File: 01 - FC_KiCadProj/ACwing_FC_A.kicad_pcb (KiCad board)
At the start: 4 copper layers, 40.8 x 40.8 mm, 111 parts, among them J1 USB-C (HRO TYPE-C-31-M-12), J2 ESC link, J3 Qwiic, J4 Qwiic, J5 ELRS, J6 ESC link B, J7 VBAT+, J8 GND, Q5 AO3401A, U1 LSM6DSV16X, U10 W25Q128JV, U11 LDK130PU-R, U12 LM5166DRCT, U13 SN74LV1T34DCKR, U2 STM32WB55CGU6, U3 IIS2MDC, U4 LPS22HH, U5 LD39130SPUR, U7 USBLC6-2SC6, U8 MLPF-WB55-01E3, Y1 32MHz

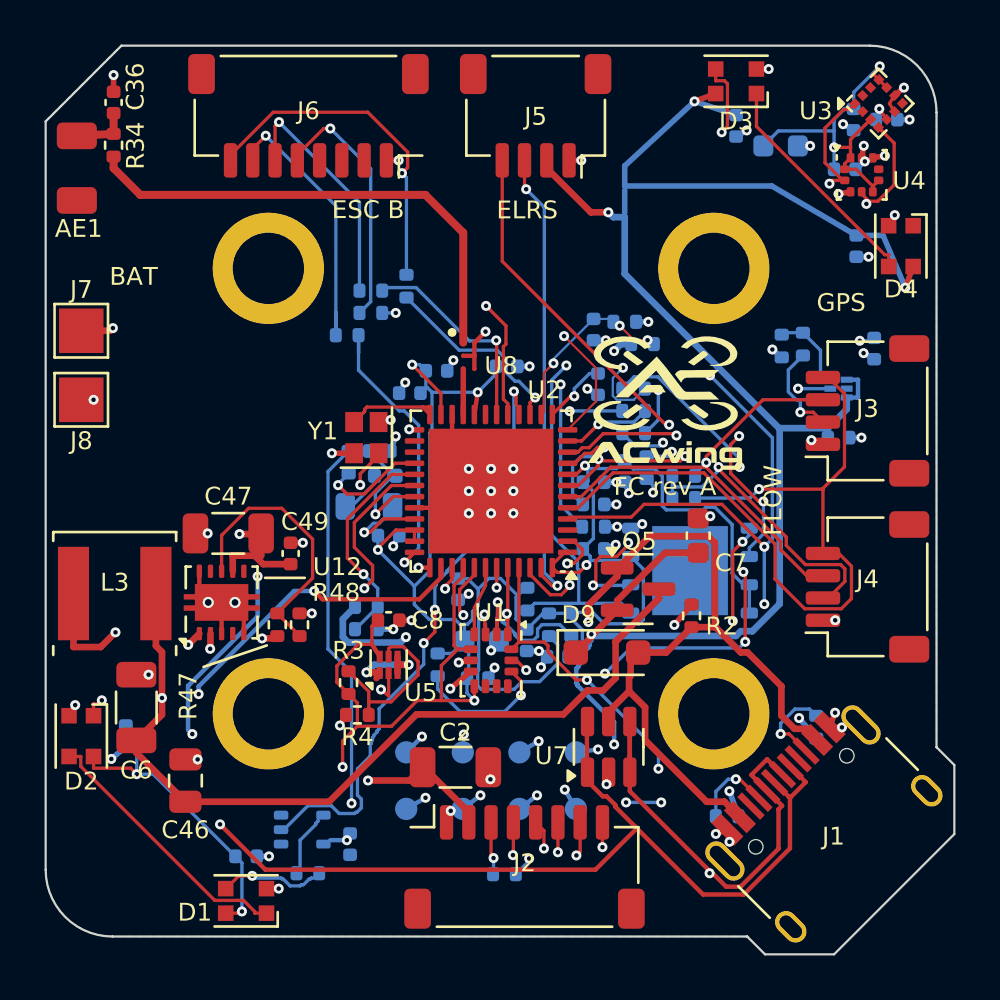
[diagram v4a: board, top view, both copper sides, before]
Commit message: Silkscreen review: board names, connector labels on the right side
- Board name + revision only, same on every board and layer: "FC rev A",
  "ESC 1S rev A", "GPS rev A", "Flow rev A" (was "ACwing ... rev A" on some).
- FC: USB and ESC A labels moved to the top (with J1 / J2); GPS and FLOW
  centred on J3 / J4; ESC B and ELRS on one line; BAT beside J7 / J8.
- Same fix on ESC 1S (CHARGE to the top, TO FC centred on J1) and GPS
  (QWIIC IN / OUT to the top, outside the SAM-M10Q outline).
- silk_brand.py: labels stay on the connector's side and never under a part;
  brand README rules updated. Gerbers, DRC (0 / 0 on all boards), views.

Co-Authored-By: Claude Opus 5.5 <noreply@anthropic.com>
Claude-Session: https://claude.ai/code/session_0189Xg6tRAL4bRZ656VQBtPX
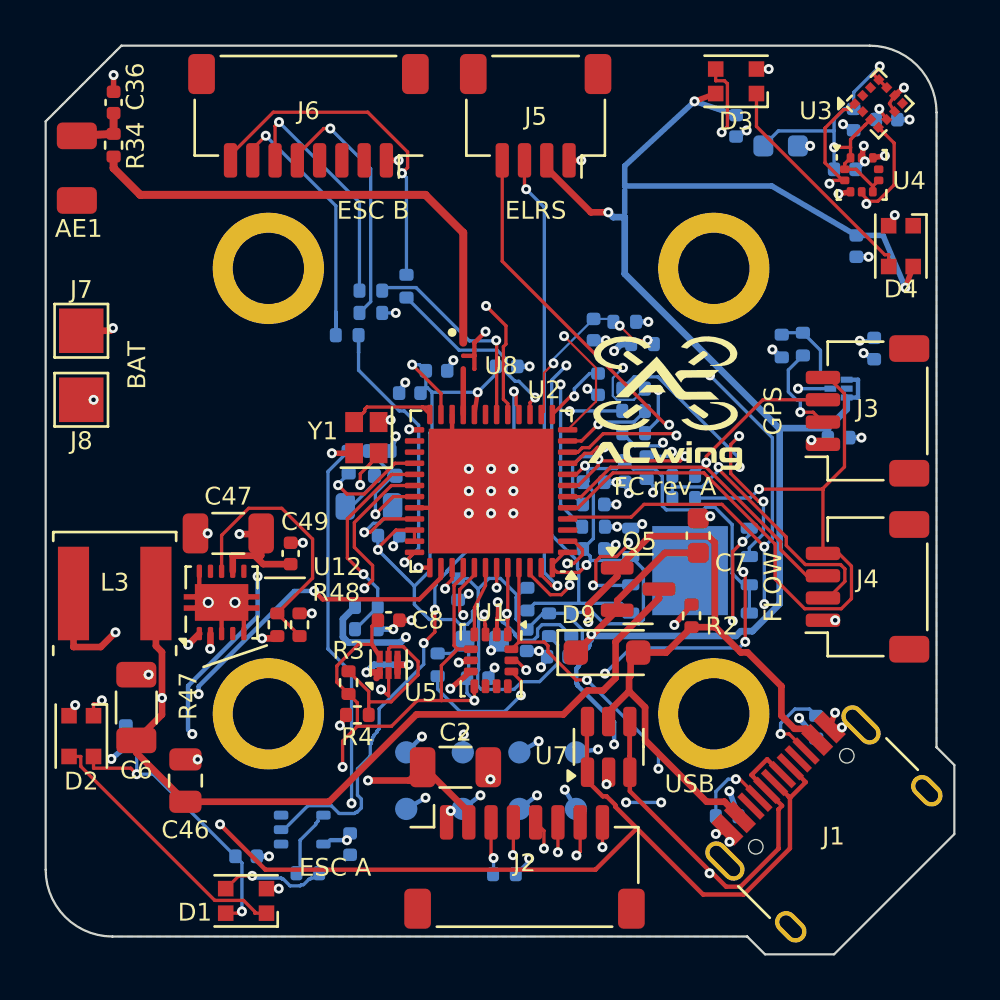
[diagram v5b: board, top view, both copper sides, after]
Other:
- board text removed: "ACwing FC rev A"
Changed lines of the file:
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@@
   (gr_line (start 170 83) (end 170 111.5)
     (stroke (width 0.1) (type default)) (layer "Edge.Cuts"))
-  (gr_text "ACwing FC rev A" (at 136.716428 106.55) (layer "B.SilkS")
+  (gr_text "FC rev A" (at 136.72 106.55) (layer "B.SilkS")
     (effects (font (size 0.8 0.8) (thickness 0.15)) (justify mirror))
   )
-  (gr_text "USB" (at 165.767 115.767) (layer "B.SilkS")
-    (effects (font (size 0.8 0.8) (thickness 0.15)) (justify mirror))
-  )
-  (gr_text "ESC A" (at 153.693587 117.375672) (layer "B.SilkS")
-    (effects (font (size 0.8 0.8) (thickness 0.15)) (justify mirror))
-  )
-  (gr_text "FLOW" (at 162.660655 100.415356 90) (layer "F.SilkS")
+  (gr_text "FLOW" (at 162.66 104.3 90) (layer "F.SilkS")
     (effects (font (size 0.8 0.8) (thickness 0.15)))
   )
-  (gr_text "ELRS" (at 151.622617 87.383211) (layer "F.SilkS")
+  (gr_text "ELRS" (at 152 87.4) (layer "F.SilkS")
     (effects (font (size 0.8 0.8) (thickness 0.15)))
   )
-  (gr_text "GPS" (at 165.717505 91.541841) (layer "F.SilkS")
+  (gr_text "USB" (at 158.915321 113.15) (layer "F.SilkS")
     (effects (font (size 0.8 0.8) (thickness 0.15)))
   )
-  (gr_text "BAT" (at 133.949999 90.366987) (layer "F.SilkS")
+  (gr_text "ESC A" (at 143 116.9) (layer "F.SilkS")
+    (effects (font (size 0.8 0.8) (thickness 0.15)))
+  )
+  (gr_text "GPS" (at 162.66 96.4 90) (layer "F.SilkS")
+    (effects (font (size 0.8 0.8) (thickness 0.15)))
+  )
+  (gr_text "BAT" (at 134.1 94.35 90) (layer "F.SilkS")
     (effects (font (size 0.8 0.8) (thickness 0.15)))
   )
@@
     (effects (font (size 0.8 0.8) (thickness 0.15)))
   )
-  (gr_text "ESC B" (at 144.479133 87.371639) (layer "F.SilkS")
+  (gr_text "ESC B" (at 144.7 87.4) (layer "F.SilkS")
     (effects (font (size 0.8 0.8) (thickness 0.15)))
   )
